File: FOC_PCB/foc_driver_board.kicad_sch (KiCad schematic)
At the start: 47 parts, among them J1 STM32-Prog-Header, J2 Conn_01x02_Pin, J3 Conn_01x06_Pin, J4 ST7796 DIsplay, J5 Conn_01x02_Pin, SW1 SW_Push, U1 MCP6007, U2 AZ1117IH-3.3, U3 AZ1117IH-5.0, U4 MCP2542FD, U5 STM32G491KEUx, U6 LSM6DSO32TR, X1 OXETDLJANF-8MHZ

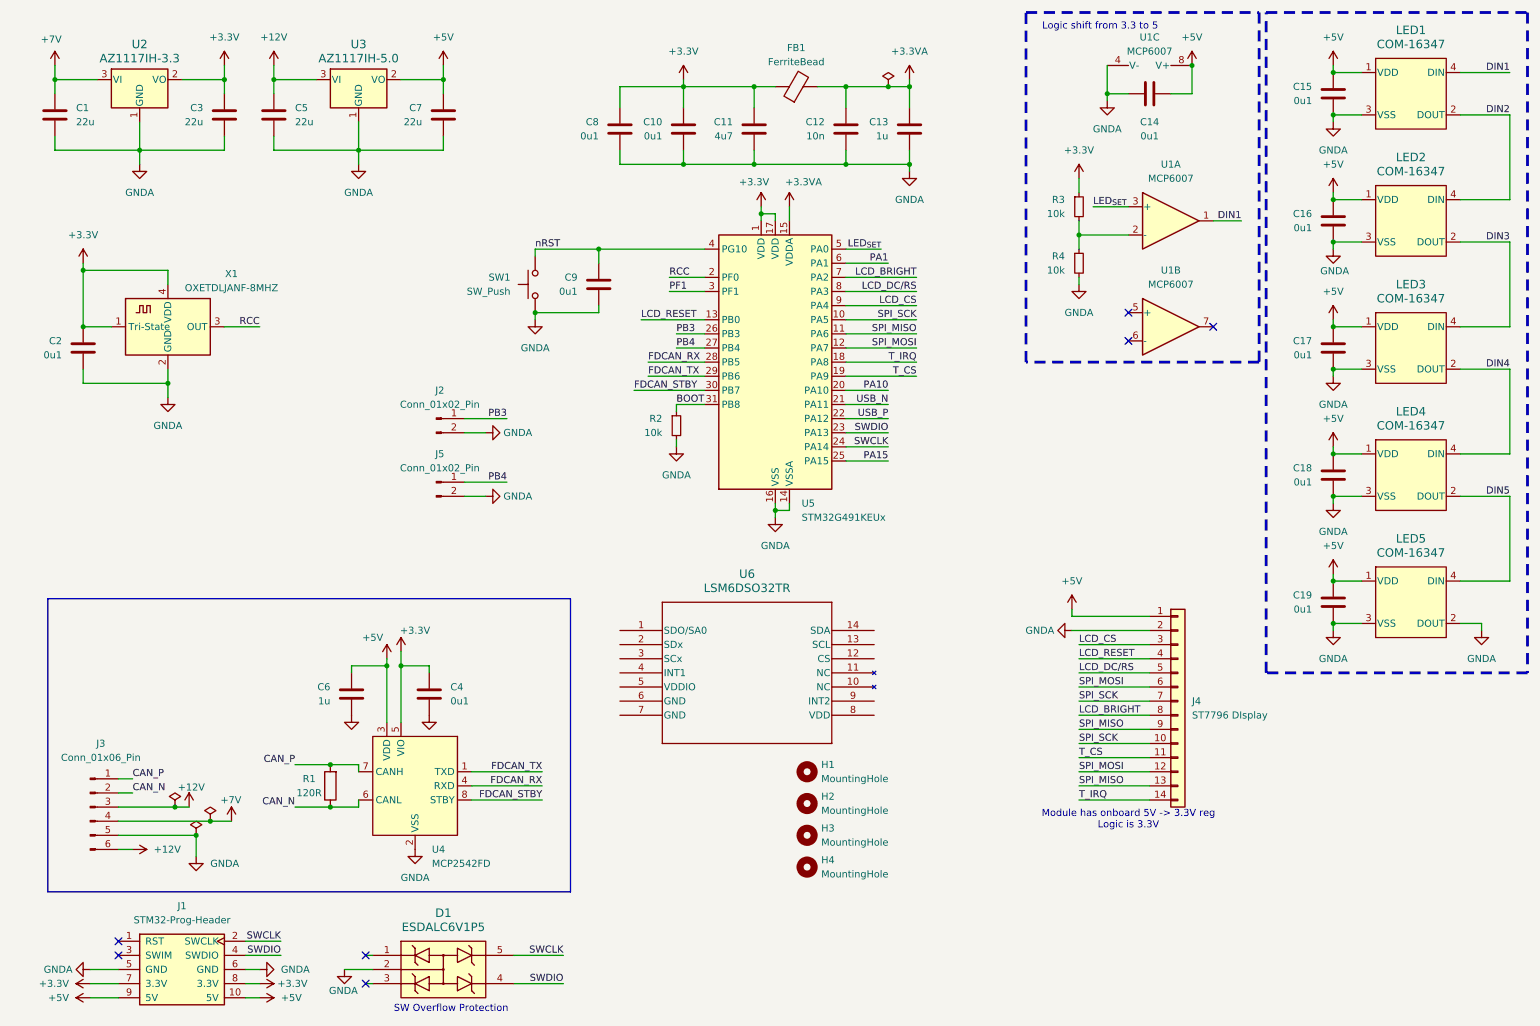
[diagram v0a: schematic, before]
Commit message: Change logic shifter to BSS138
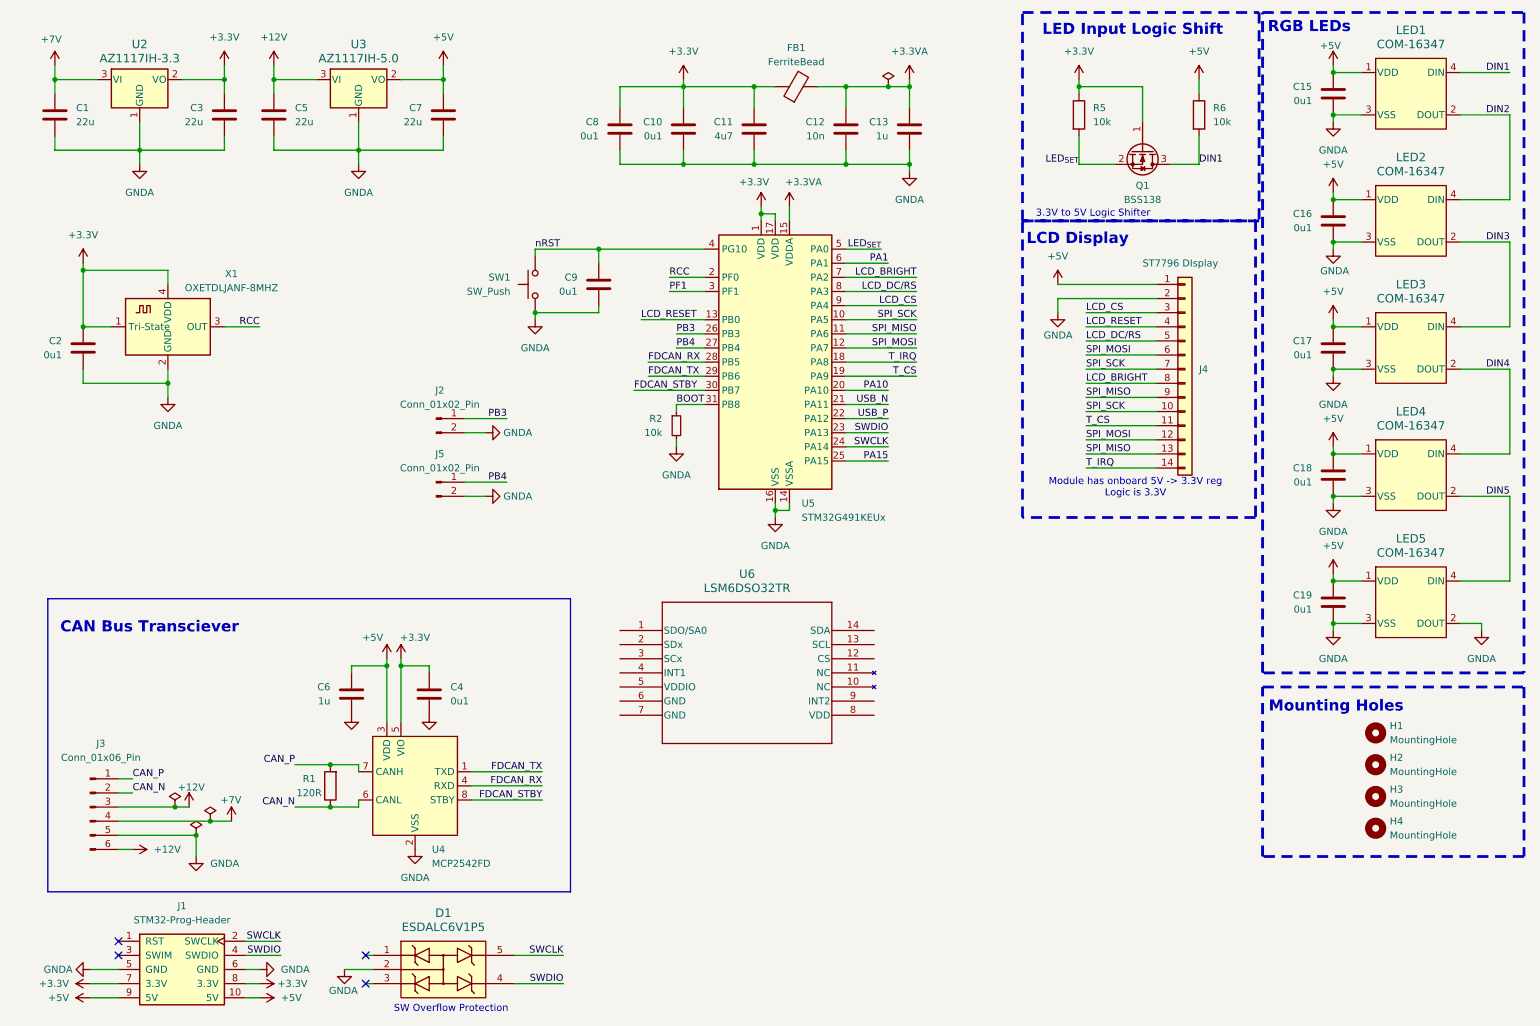
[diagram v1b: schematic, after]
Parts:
- removed C14: 0u1, Capacitor_SMD:C_0603_1608Metric, symbol Device:C
- removed R3, R4: 10k, Resistor_SMD:R_0603_1608Metric, symbol Device:R_Small
- removed U1: MCP6007, Package_SO:SOIC-8_3.9x4.9mm_P1.27mm, symbol ecocad_lib_symbols:MCP6007
- added Q1: BSS138, Package_TO_SOT_SMD:SOT-23, symbol Transistor_FET:BSS138
- added R5, R6: 10k, Resistor_SMD:R_0603_1608Metric_Pad0.98x0.95mm_HandSolder, symbol Device:R
- J4: Firmware (none) -> https://github.com/almindor/mipidsi; URL (none) -> https://www.amazon.com/Hosyond-480x320-Display-ST7796S-Mega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
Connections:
- net +3.3V: now also Q1.1 (G), R5.1
- net +5V: now also R6.1
- net DIN1: now also Q1.3 (D), R6.2
- net LED_{SET}: now also Q1.2 (S), R5.2
- no-connect marks 7 -> 4
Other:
- note added: "3.3V to 5V Logic Shifter"
- note added: "CAN Bus Transciever"
- note added: "LCD Display"
- note added: "LED Input Logic Shift"
- note added: "Mounting Holes"
- note added: "RGB LEDs"
- note removed: "Logic shift from 3.3 to 5"
- title: (none) -> FOC PCB - Dash Campbell
- moved on the sheet: H1, H2, H3, H4, J4

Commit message: PCB: Cleanup Power Symbols
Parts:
- added D2, D3: LED, LED_SMD:LED_0805_2012Metric_Pad1.15x1.40mm_HandSolder, symbol Device:LED
- added R3, R4: 4k7, Resistor_SMD:R_0603_1608Metric_Pad0.98x0.95mm_HandSolder, symbol Device:R
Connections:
- net +5V: now also R3.1
- net GNDA: now also D2.1 (K), D3.1 (K)
- net +3.3V renamed +3V3
- net +3V3: now also R4.1
- new net: D2.2 (A), R3.2
- new net: D3.2 (A), R4.2
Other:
- note added: "Power Supply"
- moved on the sheet: C1, C2, C3, C4, C5, C6, C7, J3, R1, U2, U3, U4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

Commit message: PCB: Change MCU in schematic
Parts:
- removed C10, C2, C8, C9: 0u1, Capacitor_SMD:C_0603_1608Metric, symbol Device:C
- removed C11: 4u7, Capacitor_SMD:C_0603_1608Metric, symbol Device:C
- removed C12: 10n, Capacitor_SMD:C_0603_1608Metric, symbol Device:C
- removed C13: 1u, Capacitor_SMD:C_0603_1608Metric, symbol Device:C
- removed FB1: FerriteBead, Inductor_SMD:L_0603_1608Metric, symbol Device:FerriteBead
- removed R2: 10k, Resistor_SMD:R_0603_1608Metric, symbol Device:R_Small
- removed SW1: SW_Push, Button_Switch_THT:SW_PUSH_6mm, symbol Switch:SW_Push
- removed U5: STM32G491KEUx, Package_DFN_QFN:QFN-32-1EP_5x5mm_P0.5mm_EP3.45x3.45mm, symbol MCU_ST_STM32G4:STM32G491KEUx
- removed X1: OXETDLJANF-8MHZ, Crystal:Crystal_SMD_3225-4Pin_3.2x2.5mm, symbol ecocad_lib_symbols:OXETDLJANF-8MHZ
- added C24, C25: 0u1, Capacitor_SMD:C_0603_1608Metric, symbol Device:C
- added R8, R9: 10k, Resistor_SMD:R_0603_1608Metric_Pad0.98x0.95mm_HandSolder, symbol Device:R
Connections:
- net +3V3: now also U6.2 (SDx), U6.3 (SCx), U6.5 (VDDIO), U6.8 (VDD), C24.1, C25.1, R8.1, R9.1
- net GNDA: now also U6.6 (GND), U6.7 (GND), C24.2, C25.2
- net SWO: now reaches J1.3 (SWIM)
- net IMU_SA0: now reaches U6.1 (SDO/SA0)
- net IMU_CS: now reaches U6.12 (CS)
- net IMU_SCL: now reaches U6.13 (SCL)
- net IMU_SCL: now also R9.2
- net IMU_SDA: now reaches U6.14 (SDA)
- net IMU_SDA: now also R8.2
- net IMU_INT1: now reaches U6.4 (INT1)
- net IMU_INT2: now reaches U6.9 (INT2)
- net LCD_DC/RS renamed LCD_DC
- net LED_{SET} renamed LED_IN
- net PB3 renamed BTN1
- net PB4 renamed BTN2
- no-connect marks 4 -> 3
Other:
- note added: "Current Overflow Protection"
- note added: "IMU Sensor"
- note added: "Ports"
- note removed: "SW Overflow Protection"
- company: (none) -> EcoCar CLub
- moved on the sheet: C4, C6, D1, J1, J2, J3, J5, R1, U4, U6

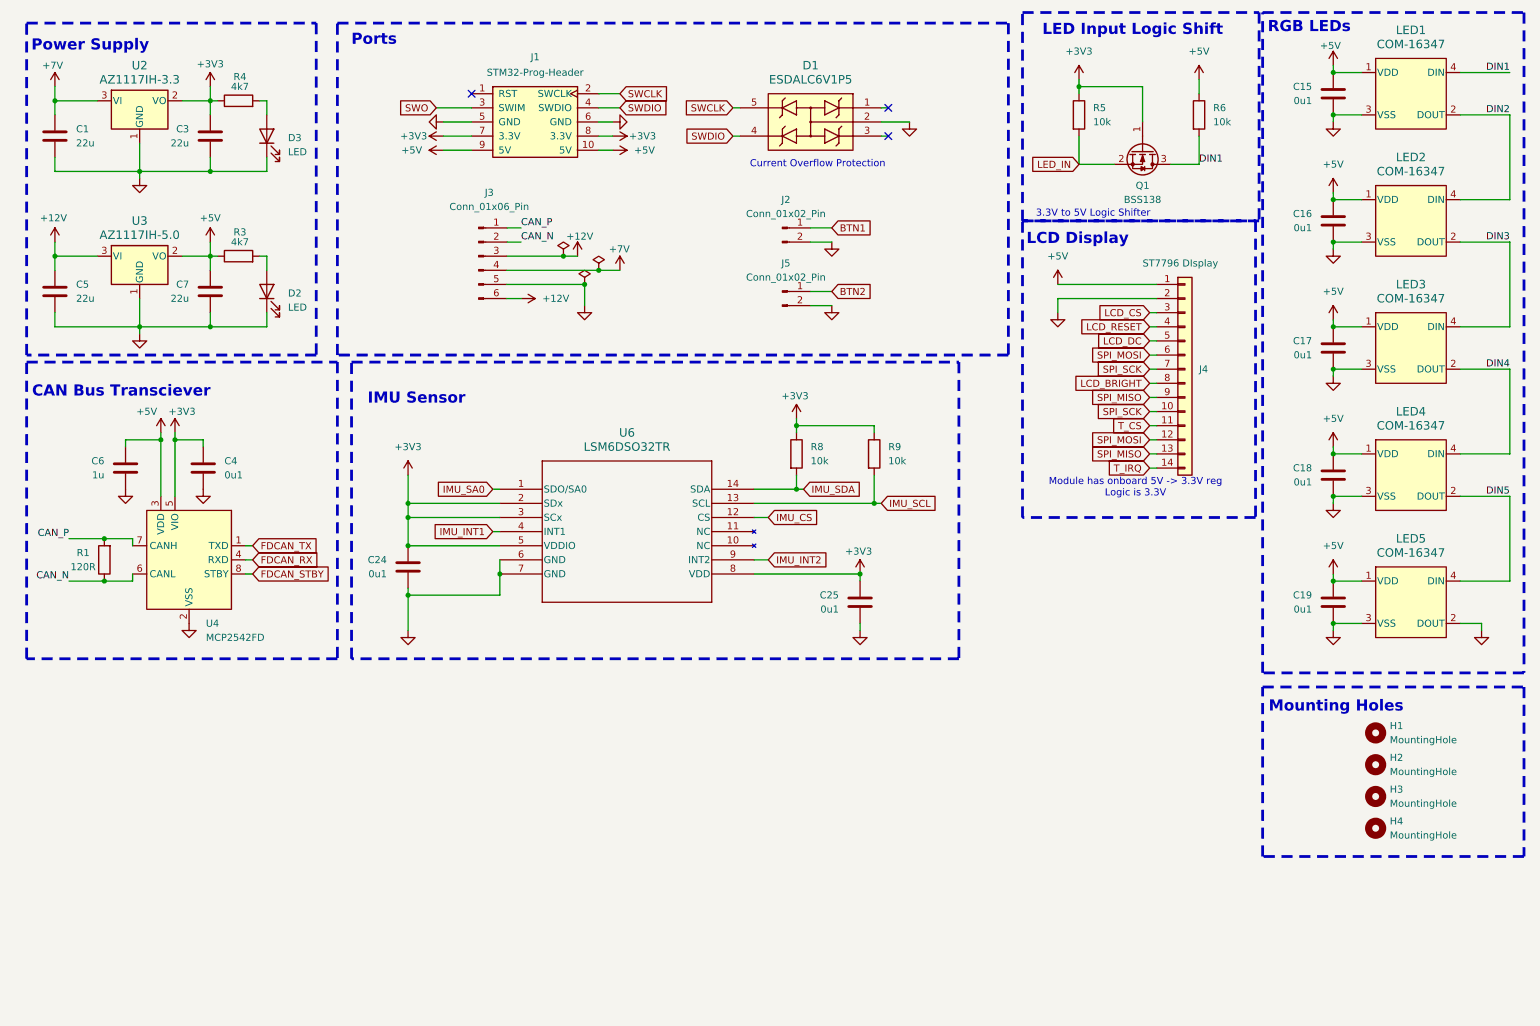
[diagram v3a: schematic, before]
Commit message: Add net class colors
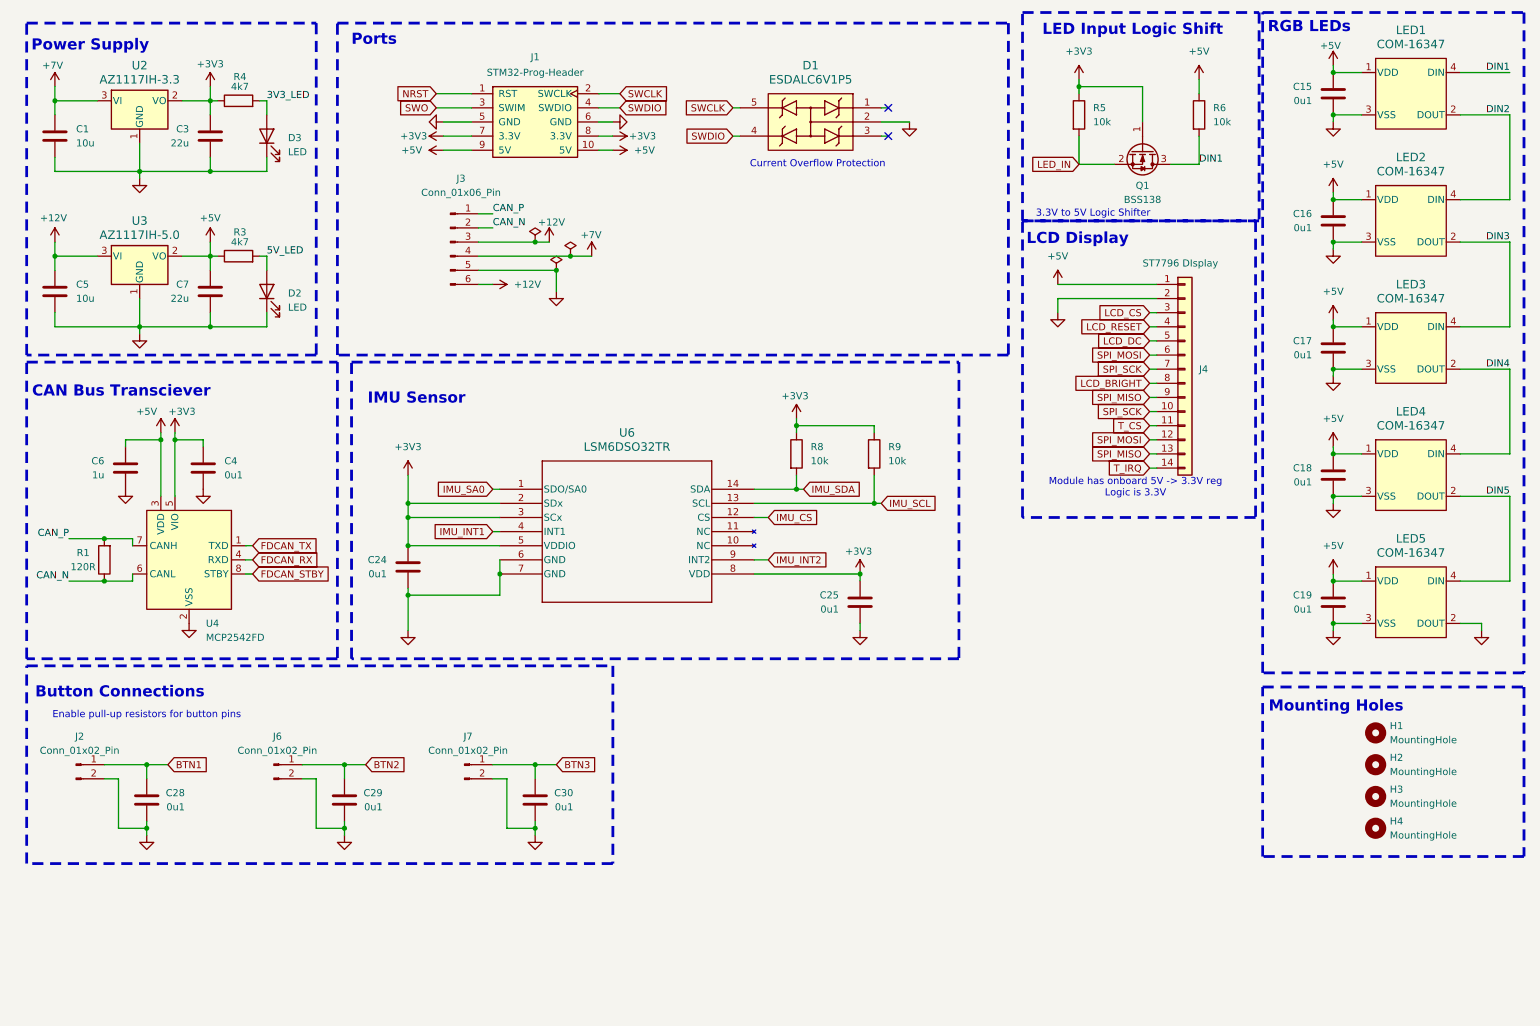
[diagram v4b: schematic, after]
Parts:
- removed J5: Conn_01x02_Pin, Connector_PinSocket_2.54mm:PinSocket_1x02_P2.54mm_Vertical, symbol Connector:Conn_01x02_Pin
- added C28, C29, C30: 0u1, Capacitor_SMD:C_0603_1608Metric_Pad1.08x0.95mm_HandSolder, symbol Device:C
- added J6, J7: Conn_01x02_Pin, Connector_PinSocket_2.54mm:PinSocket_1x02_P2.54mm_Vertical, symbol Connector:Conn_01x02_Pin
- C1, C5: value 22u -> 10u; footprint Capacitor_SMD:C_0603_1608Metric -> Capacitor_SMD:C_0805_2012Metric_Pad1.18x1.45mm_HandSolder
- C15, C16, C17, C18, C19, C24, C25, C4, C6: footprint Capacitor_SMD:C_0603_1608Metric -> Capacitor_SMD:C_0603_1608Metric_Pad1.08x0.95mm_HandSolder
- C3, C7: footprint Capacitor_SMD:C_0603_1608Metric -> Capacitor_SMD:C_0805_2012Metric_Pad1.18x1.45mm_HandSolder
- R1: footprint Resistor_SMD:R_0603_1608Metric -> Resistor_SMD:R_0603_1608Metric_Pad0.98x0.95mm_HandSolder
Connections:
- net BTN1: now also C28.1
- net BTN2: now also C29.1, J6.1 (Pin_1)
- net GNDA: now also C28.2, C29.2, C30.2, J6.2 (Pin_2), J7.2 (Pin_2)
- net 5V_LED: now reaches D2.2 (A), R3.2
- net NRST: now reaches J1.1 (RST)
- net 3V3_LED: now reaches D3.2 (A), R4.2
- new net BTN3: C30.1, J7.1 (Pin_1)
- no-connect marks 3 -> 2
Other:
- note added: "Button Connections"
- note added: "Enable pull-up resistors for button pins"
- moved on the sheet: J2, J3

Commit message: PCB: Finish layout and begin routing
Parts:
- added R10, R11, R12: 10k, Resistor_SMD:R_0603_1608Metric_Pad0.98x0.95mm_HandSolder, symbol Device:R
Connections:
- net +3V3: now also R10.1, R11.1, R12.1
- net BTN1: now also R12.2
- net BTN2: now also R11.2
- net BTN3: now also R10.2
- net CAN_N renamed FDCAN-
- net CAN_P renamed FDCAN+
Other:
- note removed: "Enable pull-up resistors for button pins"
- moved on the sheet: C28, C29, C30, J2, J6, J7
